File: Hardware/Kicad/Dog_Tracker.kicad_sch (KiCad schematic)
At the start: 21 parts, among them IC1 M4 Feather, U1 ADP160AUJZ-1.8-R7, U2 SX1280IMLTRT, U3 Origin_GPS1510, U4 NFA18SL407V1A45L, U5 SN74AUP1T97, U6 LSM6DSO32

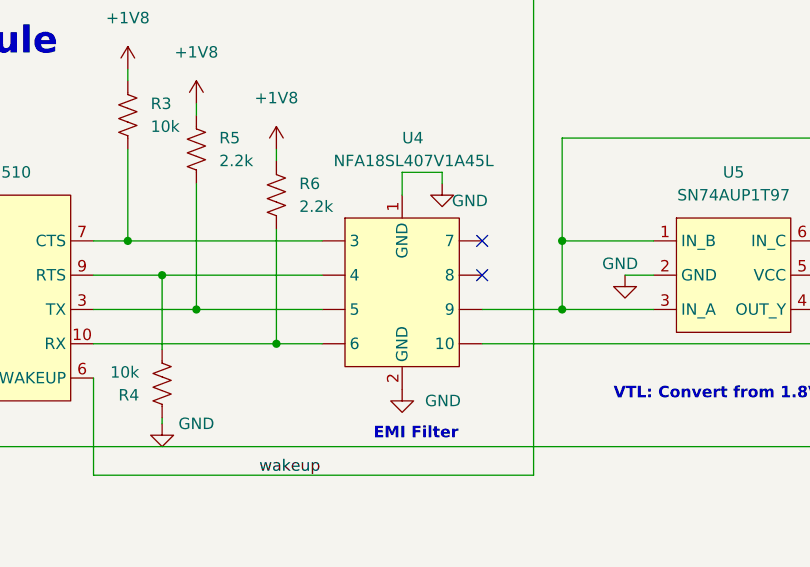
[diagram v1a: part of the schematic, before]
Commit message: fixed all footprint and added SX1280
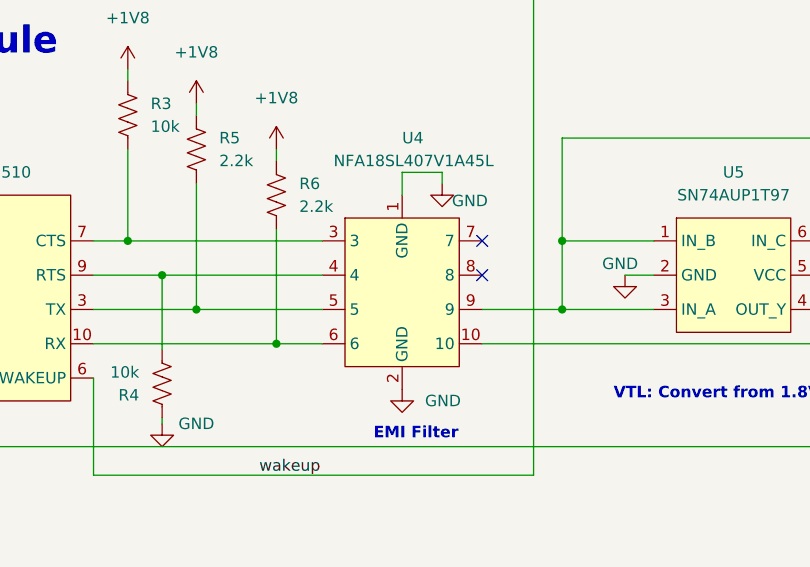
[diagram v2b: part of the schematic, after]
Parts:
- AE1: footprint (none) -> Dog_Tracker:W3211
- U2: footprint Dog_Tracker:SX1280IMLTRT -> Dog_Tracker:SX1280_Breakout
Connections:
- net I2C_SDA: now also U4.10; no longer U4. (9)
- net at R6.1, U3.10 (RX): now also U4.6; no longer U4. (9)
- net at R5.1, U3.3 (TX): now also U4.5; no longer U4. (9)
- net at R3.1, U3.7 (CTS): now also U4.3; no longer U4. (9)
- net at R4.1, U3.9 (RTS): now also U4.4; no longer U4. (9)
- net at U5.1 (IN_B), U5.3 (IN_A), U5.6 (IN_C): now also U4.9; no longer U4. (9)
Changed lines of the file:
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@@
     (property "Reference" "U2" (id 0) (at 66.675 53.975 0))
     (property "Value" "SX1280IMLTRT" (id 1) (at 66.675 38.735 0))
-    (property "Footprint" "Dog_Tracker:SX1280IMLTRT" (id 2) (at 70.485 38.735 0)
+    (property "Footprint" "Dog_Tracker:SX1280_Breakout" (id 2) (at 70.485 38.735 0)
       (effects (font (size 1.27 1.27)) hide)
     )
@@
       (effects (font (size 1.27 1.27)) (justify left))
     )
-    (property "Footprint" "" (id 2) (at 23.495 28.575 0)
+    (property "Footprint" "Dog_Tracker:W3211" (id 2) (at 23.495 28.575 0)
       (effects (font (size 1.27 1.27)) hide)
     )
@@
       (effects (font (size 1.27 1.27)) hide)
     )
-    (pin "")
-    (pin "")
-    (pin "")
-    (pin "")
-    (pin "")
-    (pin "")
-    (pin "")
-    (pin "")
-    (pin "1")
-    (pin "2")
-  )
-  (symbol (lib_id "Dog_Tracker:LSM6DSRTR") (at 82.55 75.565 0) (mirror y) (unit 1)
-    (in_bom yes) (on_board yes) (fields_autoplaced)
-    (property "Reference" "U6" (id 0) (at 83.185 65.405 0))
-    (property "Value" "LSM6DSO32" (id 1) (at 82.55 75.565 0))
-    (property "Footprint" "Dog_Tracker:LSM6DSRTR" (id 2) (at 90.17 76.835 0)
-      (effects (font (size 1.27 1.27)) hide)
-    )
-    (property "Datasheet" "" (id 3) (at 90.17 76.835 0)
-      (effects (font (size 1.27 1.27)) hide)
-    )
-    (pin "1")
     (pin "10")
-    (pin "11")
-    (pin "12")
-    (pin "13")
-    (pin "14")
-    (pin "2")
     (pin "3")
     (pin "4")
@@
     (pin "8")
     (pin "9")
+    (pin "1")
+    (pin "2")
+  )
+  (symbol (lib_id "Dog_Tracker:LSM6DSRTR") (at 82.55 75.565 0) (mirror y) (unit 1)
+    (in_bom yes) (on_board yes) (fields_autoplaced)
+    (property "Reference" "U6" (id 0) (at 83.185 65.405 0))
+    (property "Value" "LSM6DSO32" (id 1) (at 82.55 75.565 0))
+    (property "Footprint" "Dog_Tracker:LSM6DSRTR" (id 2) (at 90.17 76.835 0)
+      (effects (font (size 1.27 1.27)) hide)
+    )
+    (property "Datasheet" "" (id 3) (at 90.17 76.835 0)
+      (effects (font (size 1.27 1.27)) hide)
+    )
+    (pin "1")
+    (pin "10")
+    (pin "11")
+    (pin "12")
+    (pin "13")
+    (pin "14")
+    (pin "2")
+    (pin "3")
+    (pin "4")
+    (pin "5")
+    (pin "6")
+    (pin "7")
+    (pin "8")
+    (pin "9")
   )
   (symbol (lib_id "power:+3V3") (at 36.83 40.005 0) (unit 1)
@@
     )
     (path "/b60171e3-1072-4d20-a3d0-5c124c2b7fc1"
-      (reference "AE1") (unit 1) (value "W3211") (footprint "")
+      (reference "AE1") (unit 1) (value "W3211") (footprint "Dog_Tracker:W3211")
     )
     (path "/a82c7da7-6077-4900-b925-87315eda8158"
@@
     )
     (path "/82cef259-9dd0-43ea-9ad2-d4e5547a5601"
-      (reference "U2") (unit 1) (value "SX1280IMLTRT") (footprint "Dog_Tracker:SX1280IMLTRT")
+      (reference "U2") (unit 1) (value "SX1280IMLTRT") (footprint "Dog_Tracker:SX1280_Breakout")
     )
     (path "/49389a66-8741-452b-8284-834f65c51e1b"

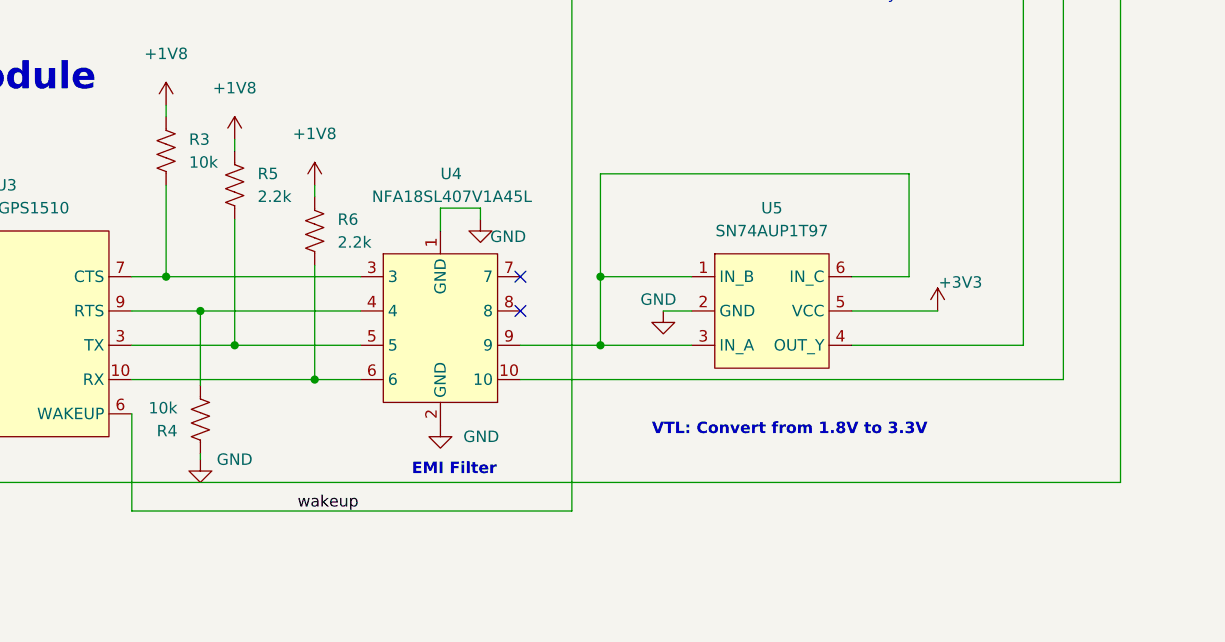
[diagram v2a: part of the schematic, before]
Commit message: 'remove emi filter and use caps'
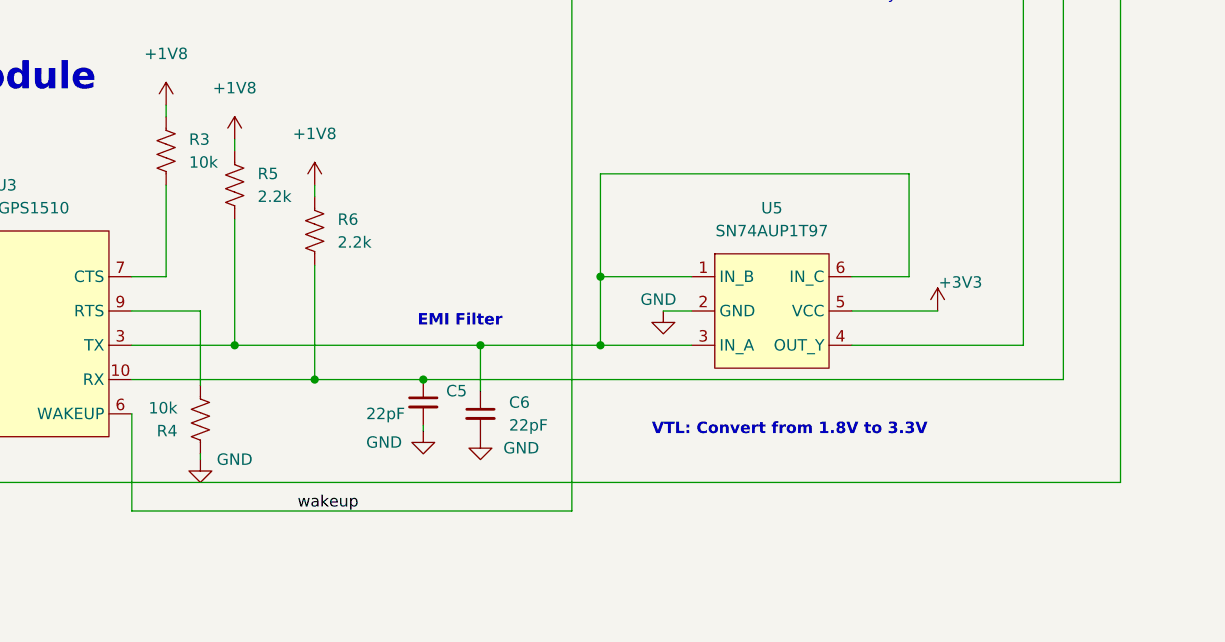
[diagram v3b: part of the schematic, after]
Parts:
- removed U4: NFA18SL407V1A45L, Dog_Tracker:NFA18SL307V1A45B, symbol Dog_Tracker:NFA18SL407V1A45L
- added C5, C6: 22pF, Capacitor_SMD:C_0402_1005Metric, symbol Device:C_Small
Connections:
- net GND: now also C5.2, C6.2
- net I2C_SDA: now also R6.1, U3.10 (RX), C5.1
- net at R5.1, U3.3 (TX): now also U5.1 (IN_B), U5.3 (IN_A), U5.6 (IN_C), C6.1
- no-connect marks 26 -> 24

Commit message: pcb check
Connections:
- net CTS: now reaches R3.1, U3.7 (CTS)
- net RTS: now reaches R4.1, U3.9 (RTS)
- net BUSY: now reaches IC1.9 (A3), U2.12 (BSY)
- net MISO: now reaches IC1.4 (MISO), U2.2 (MISO), U6.1 (SD0)
- net MOSI: now reaches IC1.5 (MOSI), U2.3 (MOSI), U6.14 (SDA)
- net SCK: now reaches IC1.6 (SCK), U2.4 (SCK), U6.13 (SCL)
- net ANT: now reaches AE1.1 (FEED), U2.9 (ANT)
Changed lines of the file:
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@@
+    (effects (font (size 1.27 1.27)) (justify left bottom))
+  )
+  (label "RTS" (at 177.165 141.605 0)
     (effects (font (size 1.27 1.27)) (justify left bottom))
   )
   (label "lora cs" (at 105.41 37.465 0)
+    (effects (font (size 1.27 1.27)) (justify left bottom))
+  )
+  (label "ANT" (at 36.83 29.845 0)
+    (effects (font (size 1.27 1.27)) (justify left bottom))
+  )
+  (label "CTS" (at 177.165 133.35 0)
+    (effects (font (size 1.27 1.27)) (justify left bottom))
+  )
+  (label "SCK" (at 93.345 40.005 0)
+    (effects (font (size 1.27 1.27)) (justify left bottom))
+  )
+  (label "SCK" (at 128.27 45.085 0)
+    (effects (font (size 1.27 1.27)) (justify left bottom))
+  )
+  (label "MISO" (at 123.825 40.005 0)
+    (effects (font (size 1.27 1.27)) (justify left bottom))
+  )
+  (label "BUSY" (at 51.435 52.705 0)
     (effects (font (size 1.27 1.27)) (justify left bottom))
   )
@@
     (effects (font (size 1.27 1.27)) (justify left bottom))
   )
+  (label "MOSI" (at 128.905 42.545 0)
+    (effects (font (size 1.27 1.27)) (justify left bottom))
+  )
